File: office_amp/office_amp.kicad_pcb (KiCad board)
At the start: 2 copper layers, 160 x 100 mm, 161 parts, among them J1 Jack-DC, J2 Conn_01x03_Female, J3 Conn_02x07_Odd_Even, J7 Screw_Terminal_01x04, J8 Conn_01x03_Female, K1 V23079-A1003-B301, K2 V23079-A1003-B301, K3 V23079-A1003-B301, K4 V23079-A1003-B301, Q1 DMT6012LSS, Q10 BSS138, Q11 BSS138, Q2 BC858, Q3 BC858, Q4 BC850, Q5 BC850, Q6 BC856, Q7 BC850, Q8 BC856, Q9 BC856, U1 LM74700, U10 DS1882E, U11 TL082, U12 TL082, U13 LM2576HVT-ADJ, U2 LM7805_TO220, U3 TL082, U4 TBA_2-2421, U5 MH-M18, U6 TPA3123D2, U7 VXO78012_TO220, U8 IL300, U9 IL300

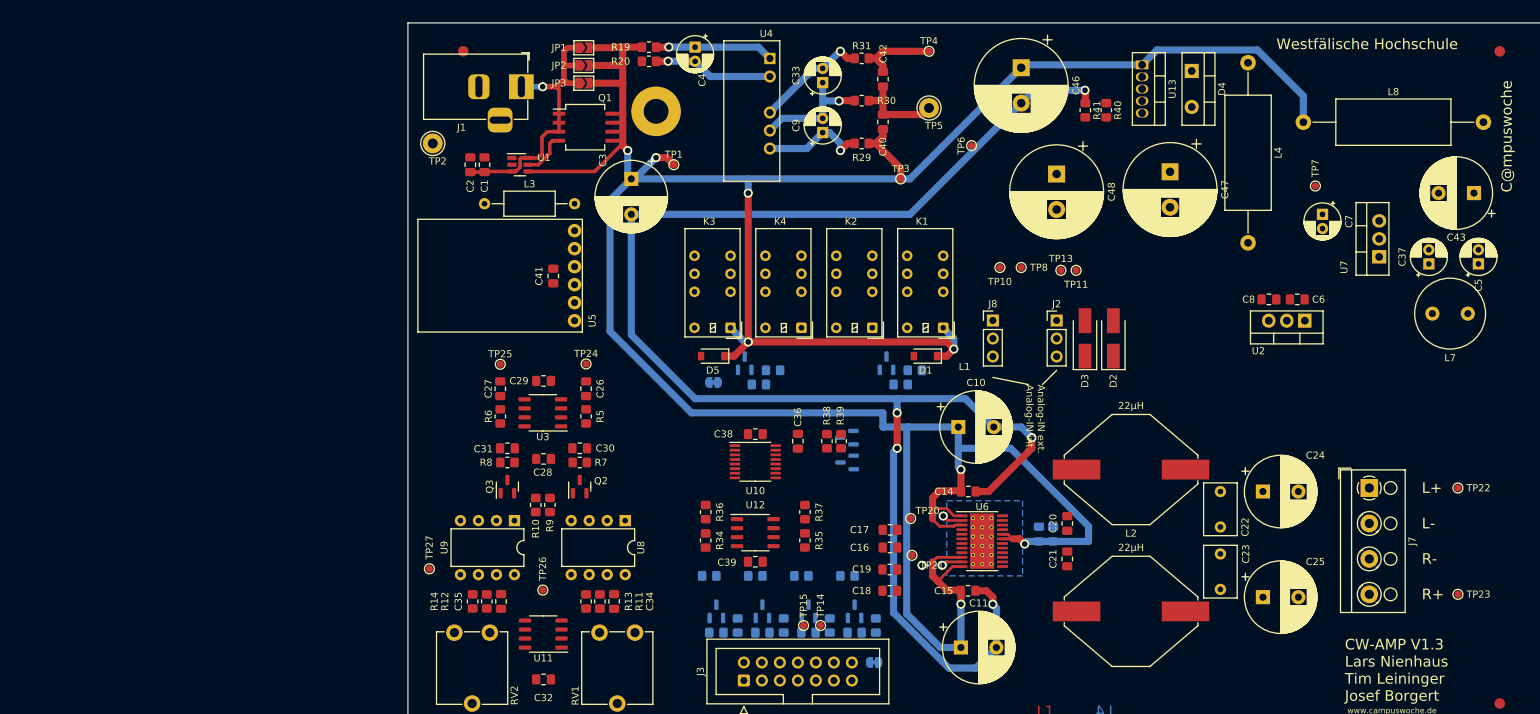
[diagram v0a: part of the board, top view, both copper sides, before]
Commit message: splitted the prototype in 2 PCBs
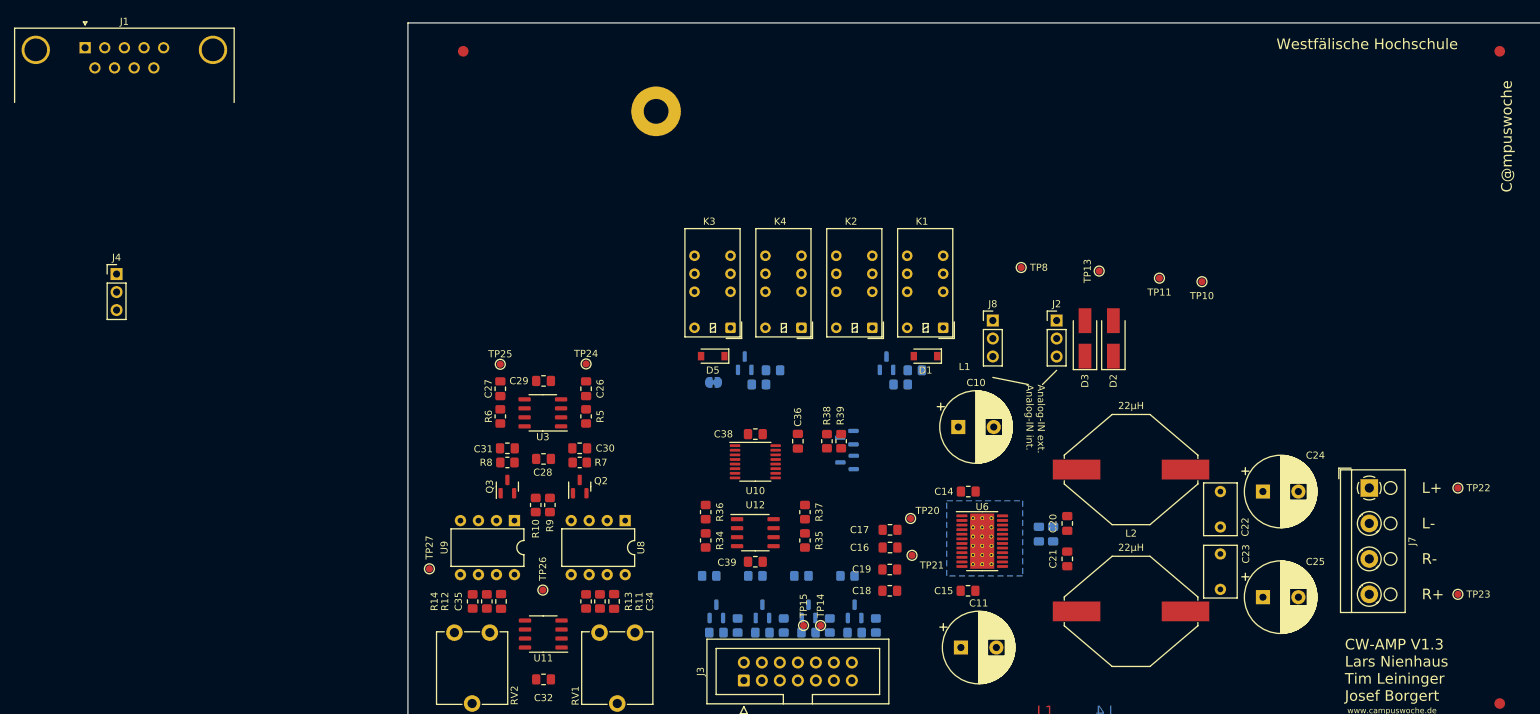
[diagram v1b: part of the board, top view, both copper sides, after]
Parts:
- removed C1: 22nF, Capacitor_SMD:C_0805_2012Metric_Pad1.18x1.45mm_HandSolder
- removed C2, C40, C42, C6, C8: 100nF, Capacitor_SMD:C_0805_2012Metric_Pad1.18x1.45mm_HandSolder
- removed C3, C43: 470µF, Capacitor_THT:CP_Radial_D10.0mm_P5.00mm
- removed C33, C4, C5, C9: 4,7µF, Capacitor_THT:CP_Radial_D5.0mm_P2.00mm
- removed C37, C7: 10µF, Capacitor_THT:CP_Radial_D5.0mm_P2.00mm
- removed C41: 10µF, Capacitor_SMD:C_0805_2012Metric_Pad1.18x1.45mm_HandSolder
- removed C46: 100µF, Capacitor_THT:CP_Radial_D13.0mm_P5.00mm
- removed C47, C48: 1000µF, Capacitor_THT:CP_Radial_D13.0mm_P5.00mm
- removed D4: 18TQ045, Package_TO_SOT_THT:TO-220-2_Vertical
- removed JP1, JP2, JP3: Jumper_2_Open, Jumper:SolderJumper-2_P1.3mm_Open_TrianglePad1.0x1.5mm
- removed L3: 100µH, Inductor_THT:L_Axial_L7.0mm_D3.3mm_P12.70mm_Horizontal_Fastron_MICC
- removed L4, L8: 56µH, Inductor_THT:L_Axial_L16.0mm_D6.3mm_P25.40mm_Horizontal_Fastron_VHBCC
- removed L7: 12µH, office_amp:L_Radial_D10.0mm_P5.00mm
- removed Q1: DMT6012LSS, MyLib:N-CH-SO-8_5.3x6.2mm_P1.27mm
- removed R19, R20: 10R, Resistor_SMD:R_0805_2012Metric_Pad1.20x1.40mm_HandSolder
- removed R29, R30, R31: 0R, Resistor_SMD:R_0805_2012Metric_Pad1.20x1.40mm_HandSolder
- removed R40: 1k, Resistor_SMD:R_0805_2012Metric_Pad1.20x1.40mm_HandSolder
- removed R41: 3k2, Resistor_SMD:R_0805_2012Metric_Pad1.20x1.40mm_HandSolder
- removed STAR3: SolderJumper_2_Bridged, Jumper:SolderJumper-2_P1.3mm_Bridged_RoundedPad1.0x1.5mm
- removed TP1, TP3, TP4, TP6, TP7: TestPoint, TestPoint:TestPoint_Pad_D1.0mm
- removed TP2, TP5: TestPoint, TestPoint:TestPoint_Loop_D2.60mm_Drill1.4mm_Beaded
- removed U1: LM74700, Package_TO_SOT_SMD:SOT-23-6
- removed U13: LM2576HVT-ADJ, Package_TO_SOT_THT:TO-220-5_Vertical
- removed U2: LM7805_TO220, Package_TO_SOT_THT:TO-220-3_Vertical
- removed U4: TBA_2-2421, office_amp:SIP-7
- removed U5: MH-M18, MyLib:MH-M18
- removed U7: VXO78012_TO220, Package_TO_SOT_THT:TO-220-3_Vertical
- added J4: Conn_01x03_Female, Connector_PinHeader_2.54mm:PinHeader_1x03_P2.54mm_Vertical, F.Cu at (48.9, 93.4)
- J1: value Jack-DC -> Conn_01x09_Socket; footprint Connector_BarrelJack:BarrelJack_Horizontal -> Connector_Dsub:DSUB-9_Male_Horizontal_P2.77x2.84mm_EdgePinOffset4.94mm_Housed_MountingHolesOffset7.48mm
- moved J1 61.8 mm to (44.5, 61.5)
- moved TP10 28.6 mm to (202.0, 94.5)
- moved TP11 11.8 mm to (196.0, 94.0)
- moved TP13 5.40 mm to (187.5, 93.0), turned to 0 degrees
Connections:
- D1 pad 2: V+ -> Net-(D1-A)
- J1 pad 1: /Power/Vin -> GNDREF
- J1 pad 2: GNDREF -> V+
- J1 pad 3: (no net) -> +12V
- J3 pad 11: BT-MUTE -> unconnected-(J3-Pin_11-Pad11)
- J3 pad 9: BT-KEY -> unconnected-(J3-Pin_9-Pad9)
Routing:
- net V+: track 444.2 -> 0.00 mm, vias 8 -> 0
- net GNDREF: track 224.0 -> 0.00 mm, vias 5 -> 0
- net /Power/Vin: track 40.5 -> 0.00 mm, vias 1 -> 0
- net Net-(U4-Common): track 17.8 -> 0.00 mm, vias 1 -> 0
- net Net-(U4--VIN): track 17.0 -> 0.00 mm, vias 1 -> 0
- net Net-(U4-+VIN): track 16.7 -> 0.00 mm, vias 1 -> 0
- net Net-(U4--VOUT): track 15.9 -> 0.00 mm, vias 1 -> 0
- net Net-(U4-+VOUT): track 14.9 -> 0.00 mm, vias 1 -> 0
- net GND_Input: track 12.9 -> 0.00 mm
- net -5VA: track 11.2 -> 0.00 mm
- net +5VA: track 9.86 -> 0.00 mm
- net Net-(U1-GATE): track 6.58 -> 0.00 mm
- net /Class_D/VCLAMP: track 5.83 -> 0.00 mm, vias 2 -> 0
- net /Class_D/~{SD}: track 2.90 -> 0.00 mm, vias 1 -> 0

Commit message: first positioning office-amp
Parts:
- removed REF**: MountingHole_3.5mm_Pad, MountingHole:MountingHole_3.5mm_Pad
- moved J4 145.3 mm to (194.2, 94.5), turned to -90 degrees
- moved J1 56.5 mm to (97.9, 80.0), turned to -90 degrees
- moved R26 52.3 mm to (104.7, 153.0), turned to 0 degrees
- moved C34 50.6 mm to (143.6, 95.3)
- moved Q2 50.6 mm to (138.7, 79.1)
- moved Q3 50.6 mm to (128.5, 79.1)
- moved R11 50.6 mm to (141.6, 95.3)
- moved RV2 50.6 mm to (121.0, 99.7)
- moved C26 50.6 mm to (139.6, 65.3)
- moved C27 50.6 mm to (127.5, 65.3)
- moved C28 50.6 mm to (133.6, 75.2)
- moved C29 50.6 mm to (133.6, 64.2)
- moved C30 50.6 mm to (138.7, 73.7)
- moved C31 50.6 mm to (128.5, 73.7)
- moved C32 50.6 mm to (133.6, 106.3)
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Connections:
- J1 pad 1: GNDREF -> -5V
- J1 pad 2: V+ -> +5V
- J1 pad 4: +5V -> GNDREF
- J1 pad 5: -5V -> V+
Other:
- board text removed: "L1"
- board text removed: "L4"

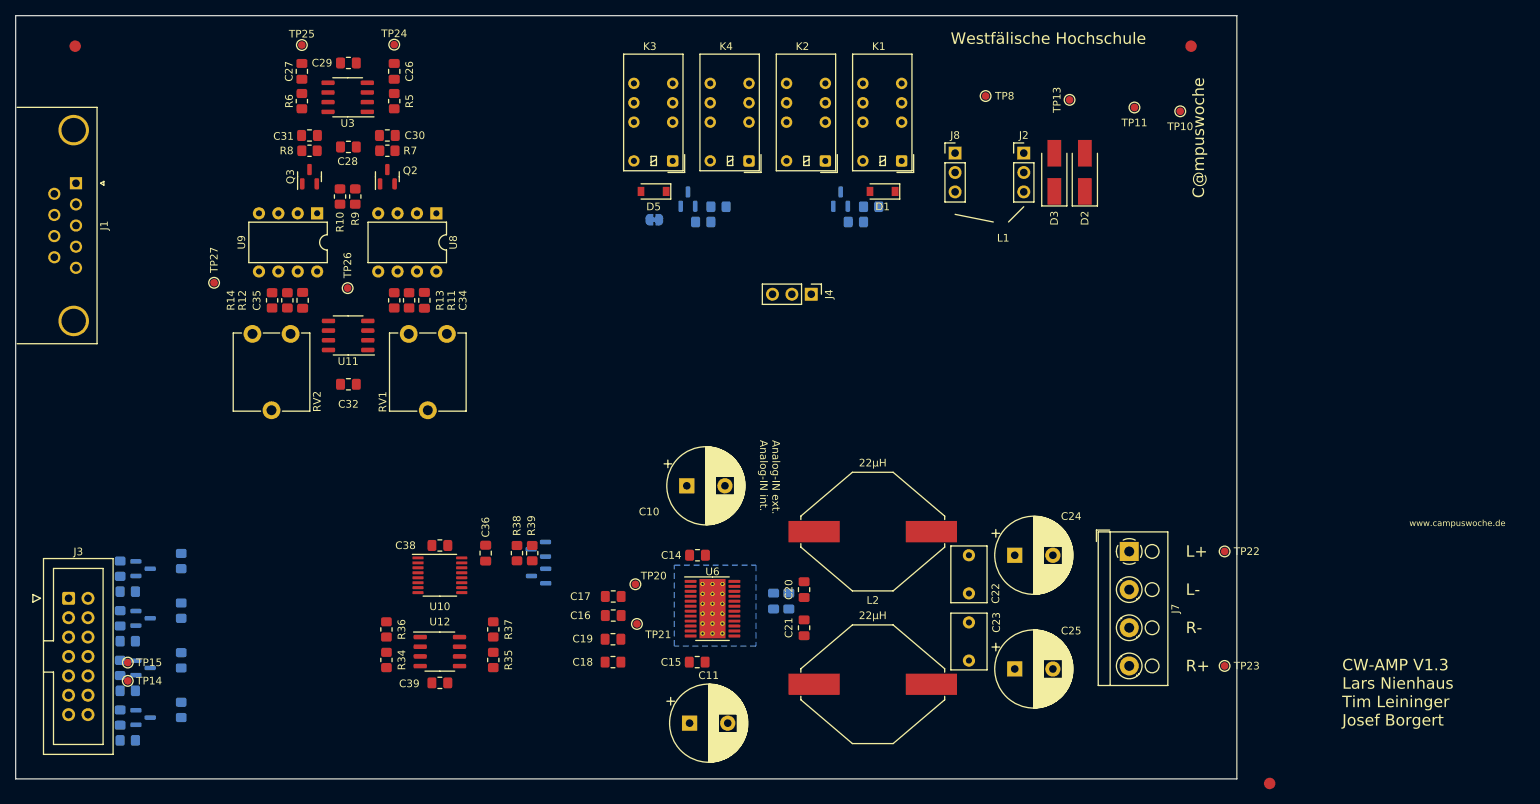
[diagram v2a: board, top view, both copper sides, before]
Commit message: Layout Amp done
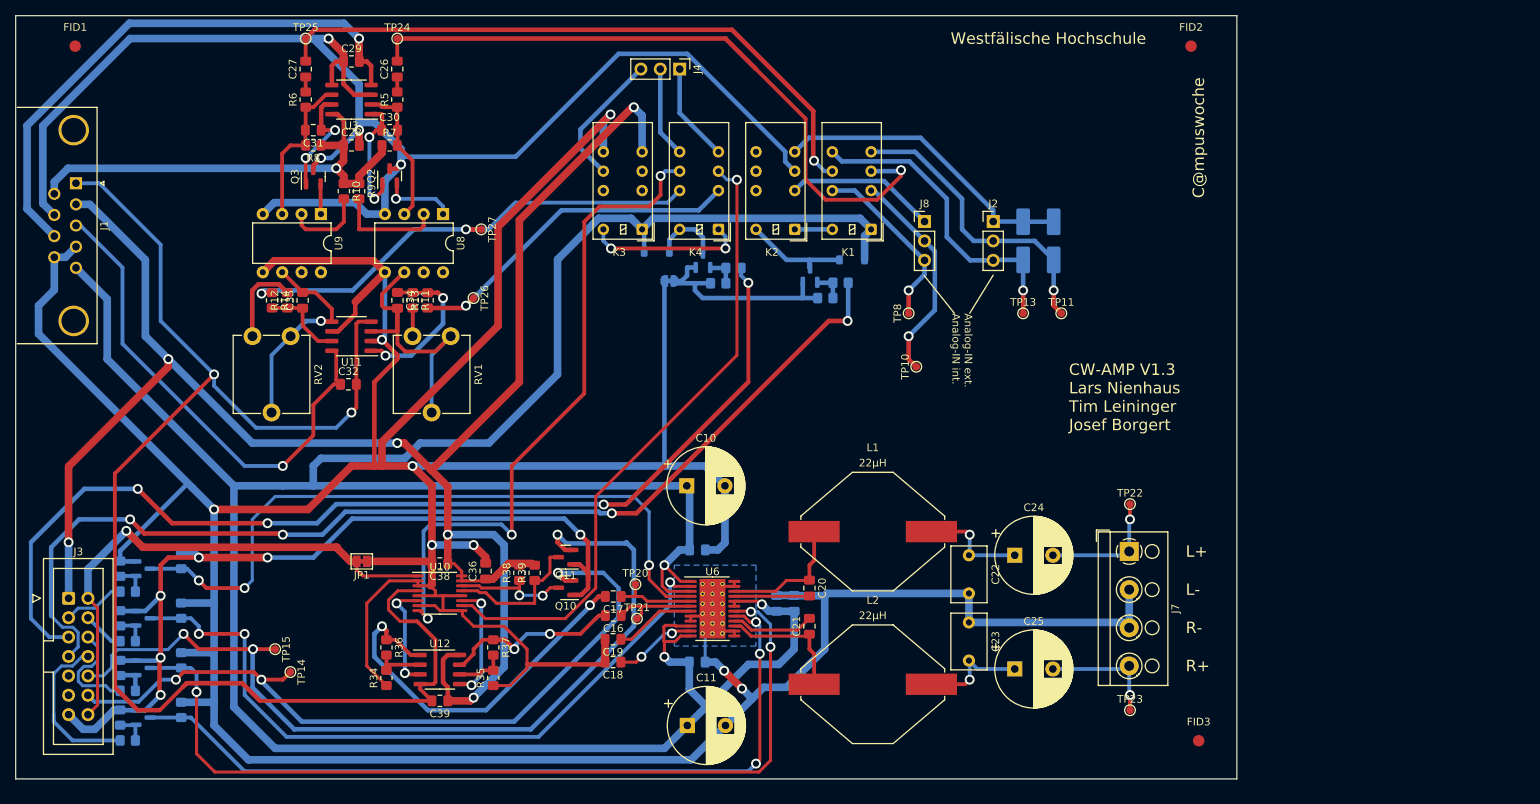
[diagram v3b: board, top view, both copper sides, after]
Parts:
- added JP1: Jumper_2_Bridged, Jumper:SolderJumper-2_P1.3mm_Bridged_Pad1.0x1.5mm, F.Cu at (135.3, 129.5)
- C14, C15, D1, D2, D3, D5: moved to B.Cu
- Q10, Q11: moved to F.Cu
- moved TP10 48.1 mm to (208.0, 104.0)
- moved TP27 35.7 mm to (151.0, 86.0)
- moved J4 34.2 mm to (177.0, 65.0)
- moved TP8 30.2 mm to (207.0, 97.0)
- moved TP13 28.6 mm to (222.0, 97.0)
- moved TP11 28.6 mm to (227.0, 97.0)
- moved TP14 21.3 mm to (126.0, 144.0)
- moved TP15 19.4 mm to (124.0, 141.0)
- moved TP26 16.6 mm to (150.0, 95.0)
- moved TP22 13.9 mm to (236.0, 122.0)
- moved TP23 13.7 mm to (236.0, 149.0)
- moved FID3 10.9 mm to (245.0, 153.0)
- moved Q4 10.7 mm to (194.1, 92.0)
- moved R15 10.7 mm to (198.1, 93.0)
- moved R16 10.7 mm to (196.1, 95.0)
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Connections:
- J1 pad 9: unconnected-(J1-Pin_9-Pad9) -> GNDREF
- U10 pad 1: GNDREF -> GNDD
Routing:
- net GNDREF: track 0.00 -> 604.8 mm, vias 0 -> 8
- net V+: track 0.00 -> 372.4 mm, vias 0 -> 3
- net +5V: track 0.00 -> 236.6 mm, vias 0 -> 6
- net GND_Input: track 0.00 -> 195.3 mm, vias 0 -> 4
- net -5V: track 0.00 -> 186.4 mm, vias 0 -> 2
- net SELECT-Analog: track 0.00 -> 140.6 mm, vias 0 -> 4
- net SELECT-BT: track 0.00 -> 137.7 mm, vias 0 -> 4
- net +3V3: track 0.00 -> 117.7 mm, vias 0 -> 6
- net /Class_D/GAIN0: track 0.00 -> 117.1 mm, vias 0 -> 3
- net /Class_D/SDA: track 0.00 -> 115.8 mm, vias 0 -> 3
- net /Class_D/GAIN1: track 0.00 -> 104.8 mm, vias 0 -> 3
- net /Class_D/SCL: track 0.00 -> 99.2 mm, vias 0 -> 3
- net /Class_D/~{SD}: track 0.00 -> 92.9 mm, vias 0 -> 3
- net /Class_D/MUTE: track 0.00 -> 92.1 mm, vias 0 -> 3
- net /Audio_Isolation/R-In-ISO: track 0.00 -> 88.4 mm, vias 0 -> 1
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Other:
- board text removed: "42Volt.de"
- board text removed: "www.campuswoche.de"

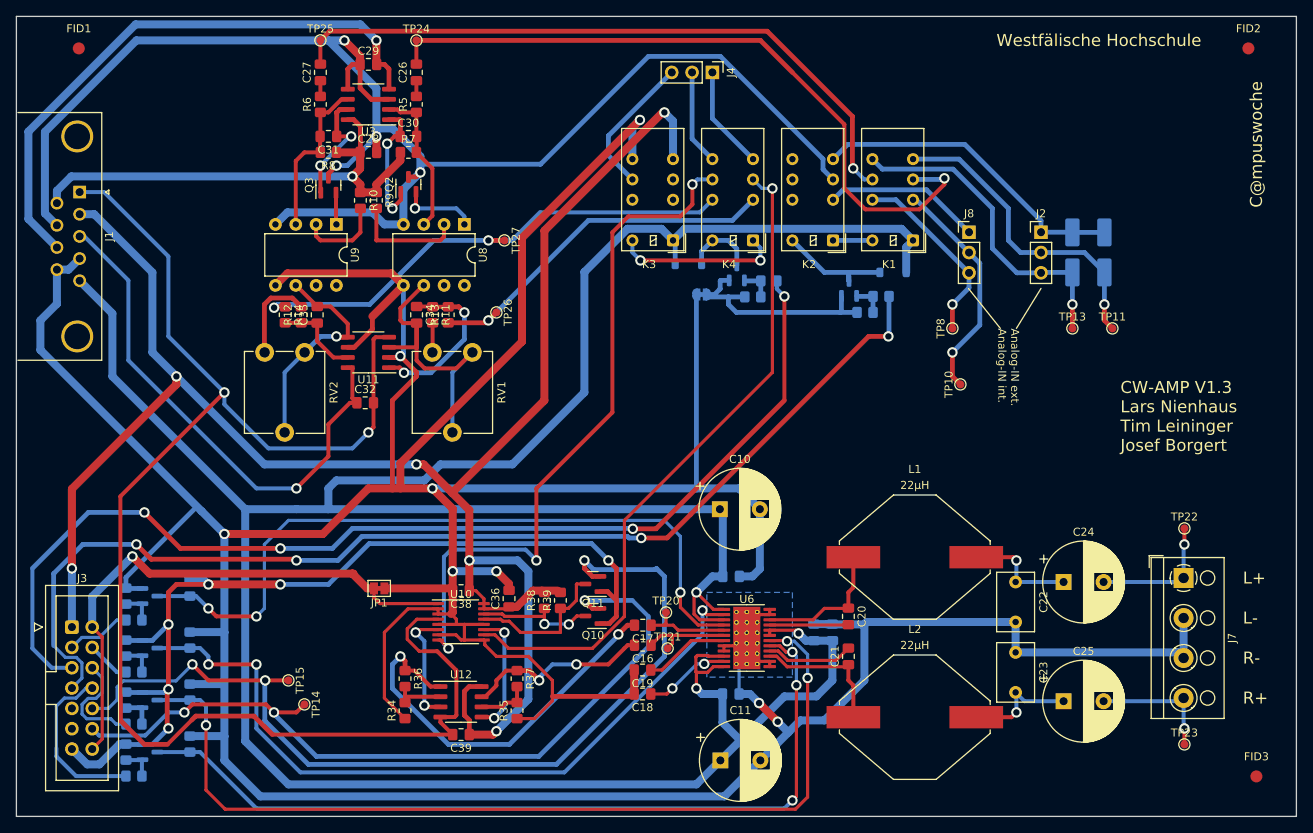
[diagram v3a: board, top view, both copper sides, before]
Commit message: Layout Amp done
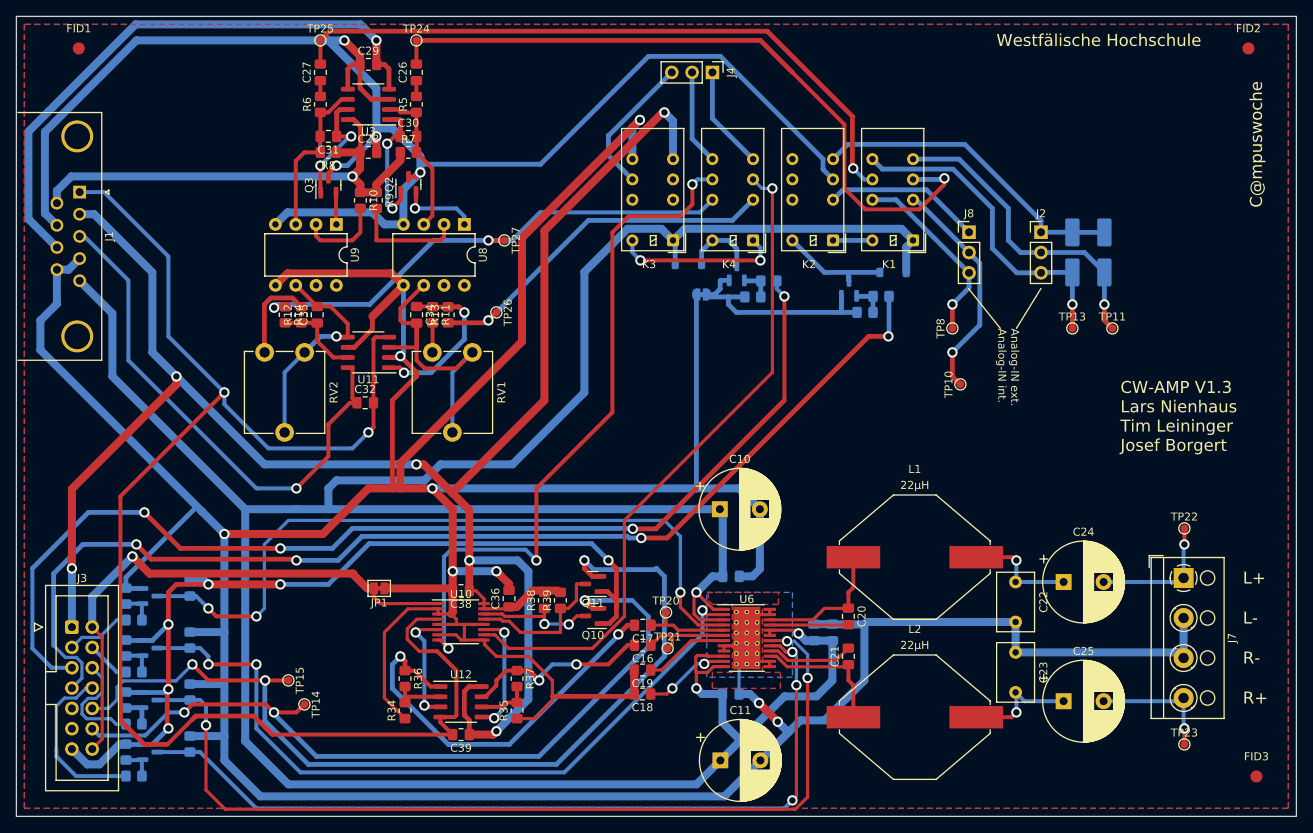
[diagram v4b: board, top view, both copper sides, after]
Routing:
- added copper zone on F.Cu, net GNDREF
